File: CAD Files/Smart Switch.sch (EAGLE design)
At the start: 27 parts, among them IC1 78L05Z, X1 MKDSN1,5/3-5,08

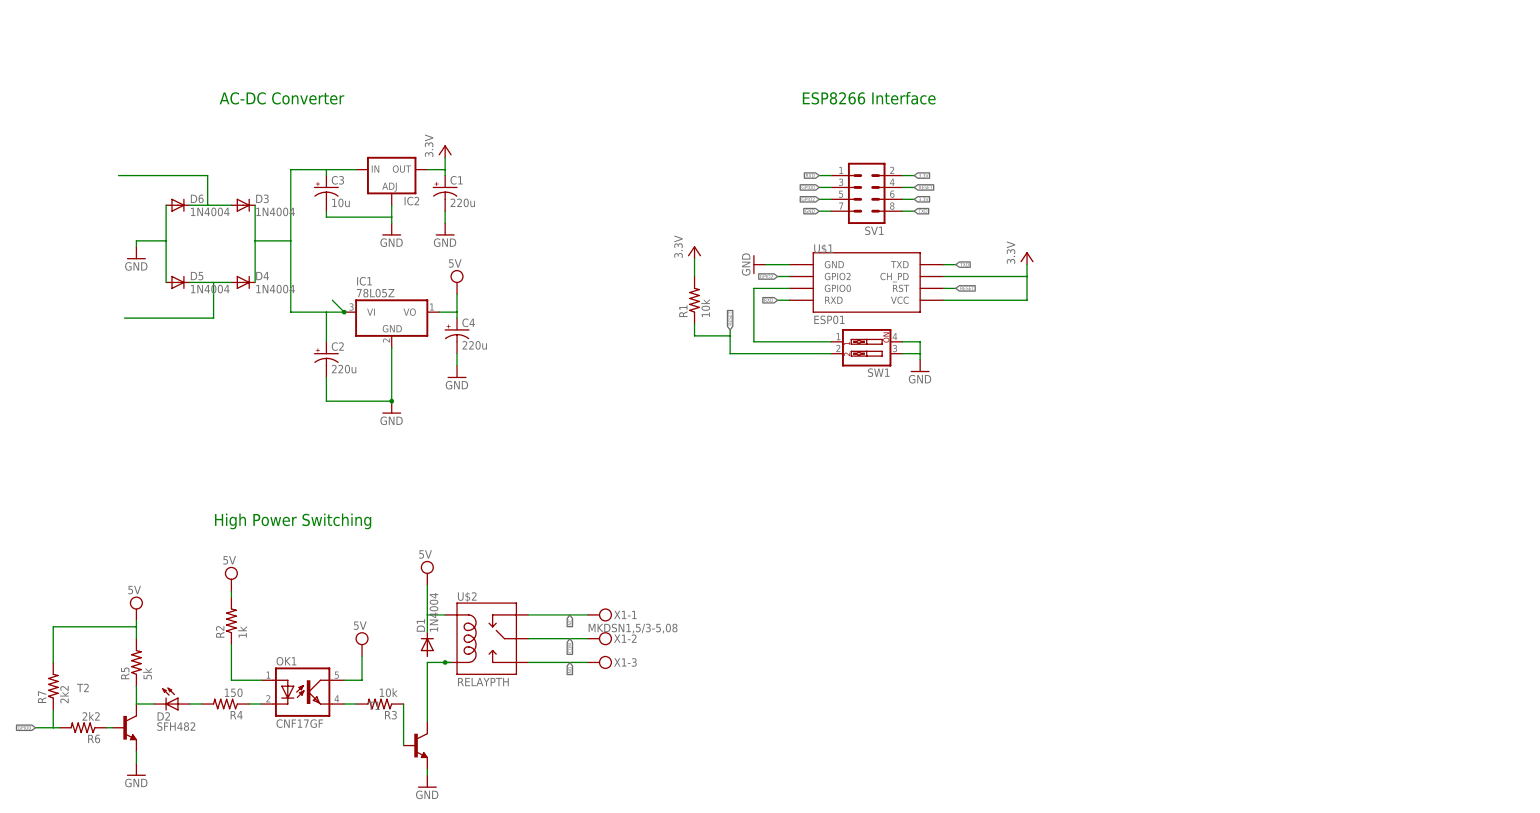
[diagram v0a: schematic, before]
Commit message: Added final schematic and board layout
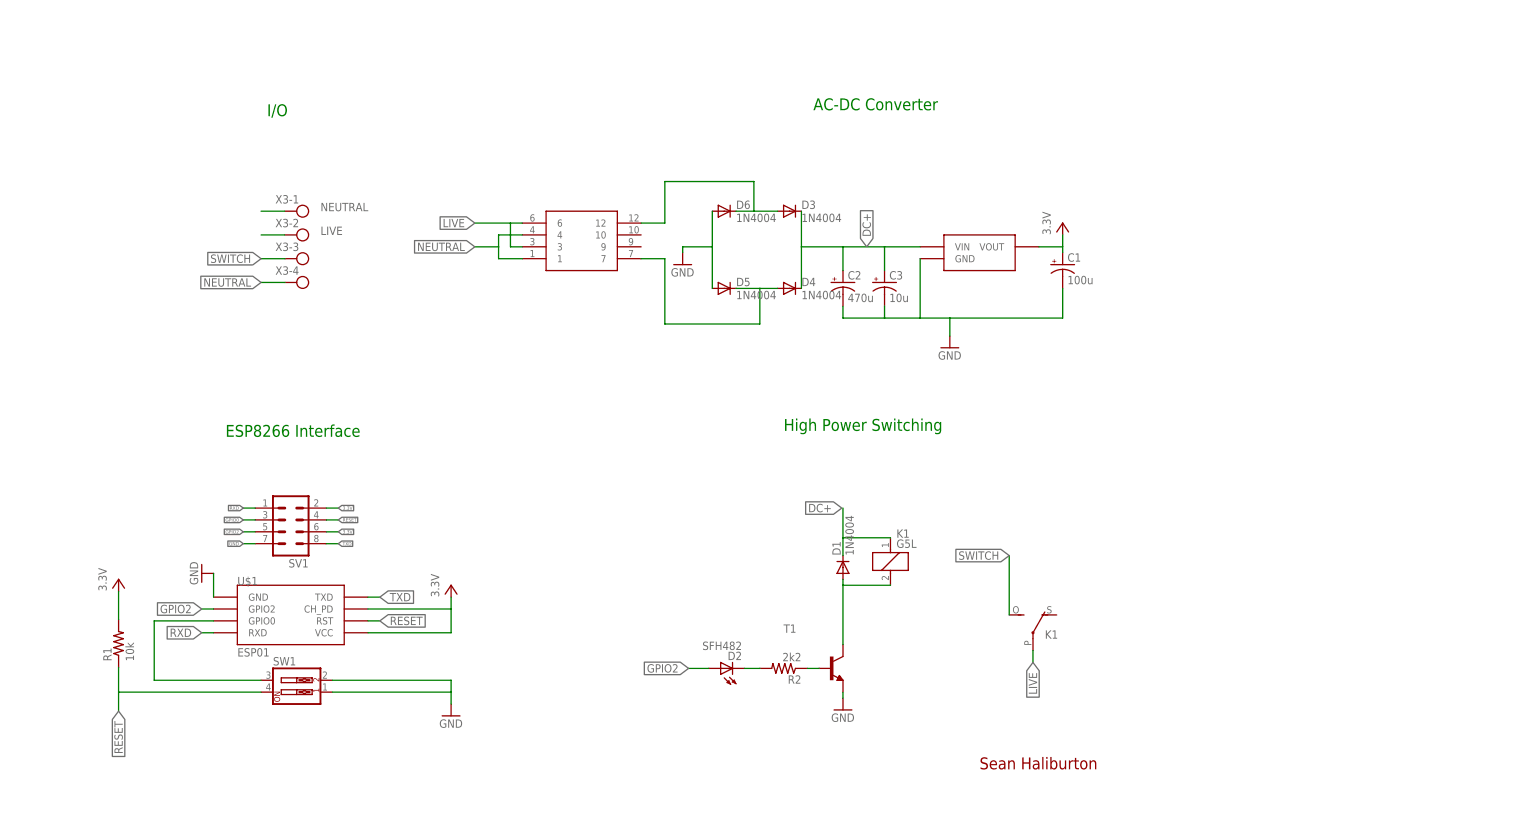
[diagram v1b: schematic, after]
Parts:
- removed C4: 220u, resistor:CPOL-USE2.5-6
- removed IC1: 78L05Z, linear:78L05Z
- removed IC2: (no value), v-reg:LM138-TL
- removed OK1: CNF17GF, optocoupler:CNF17GF
- removed R3: 10k, rcl:R-US_0411/15
- removed R4: 150, rcl:R-US_0411/15
- removed R5: 5k, rcl:R-US_0411/15
- removed R6, R7: 2k2, rcl:R-US_0411/15
- removed T2: (no value), transistor-neu-to92:2N2222-NPN-TO92-EBC
- removed X1: MKDSN1,5/3-5,08, con-phoenix-508:MKDSN1,5/3-5,08
- added K1: G5L, relay:G5L
- added U$3: CL2-10R-12, smart-switch:CL2-10R-12
- added X3: MKDSN1,5/4-5,08, con-phoenix-508:MKDSN1,5/4-5,08
- C1: value 220u -> 100u
- C2: value 220u -> 470u
- R1: device rcl:R-US_0411/15 -> rcl:R-US_0204/7
- R2: value 1k -> 2k2; device rcl:R-US_0411/15 -> rcl:R-US_0204/7
- U$2: value RELAYPTH -> ZLDO1117; device SRD-05VDC-SL-C:RELAYPTH -> smart-switch:ZLDO1117
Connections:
- removed net 3.3V1: C4.+
- removed net 5V: D1.C, IC1.VO, OK1.COL, R2.2, R5.2, R7.2, U$2.COIL1
- removed net COM: U$2.SWCOMMON, X1-2.KL
- removed net N$11: D3.A, D6.C
- removed net N$2: R3.1, T1.B
- removed net N$4: OK1.A, R2.1
- removed net N$6: OK1.C, R4.1
- removed net N$7: R6.1, T2.B
- removed net N$8: D4.A, D5.C
- removed net NC: U$2.SWCLOSE, X1-1.KL
- removed net NO: U$2.SWOPEN, X1-3.KL
- removed net X: D2.C, R5.1, T2.C
- new net LIVE: K12.P, U$3.3, U$3.6, X3-2.KL
- new net NEUTRAL: U$3.1, U$3.4, X3-1.KL, X3-4.KL
- new net SEC1: D3.A, D6.C, U$3.12
- new net SEC2: D4.A, D5.C, U$3.7
- new net SWITCH: K12.S, X3-3.KL
- net 3.3V: now also U$2.VOUT; no longer IC2.OUT
- net DC+: now also D1.C, K11.1, U$2.VIN; no longer IC1.VI, IC2.IN
- net GND: now also SW1.1, SW1.2, U$2.GND; no longer C4.-, IC1.GND, IC2.ADJ, SW1.3, SW1.4, T2.E
- net GPIO0: now also SW1.3; no longer R6.2, R7.1, SW1.1
- net GPIO2: now also D2.A
- net N$1: now also R2.1, T1.B; no longer OK1.EMIT, R3.2
- net N$3: now also D1.A, K11.2; no longer U$2.COIL0
- net N$5: now also D2.C, R2.2; no longer D2.A, R4.2
- net RESET: now also SW1.4; no longer SW1.2
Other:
- note added: "I/O"
- note added: "Sean Haliburton"
- moved on the sheet: C1, C2, C3, D1, D2, D3, D4, D5, D6, R1, R2, SV1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

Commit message: Changed most of the design
Replaced relay with triac and opto isolator
Replaced transformer with alternative AC-DC converter
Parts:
- removed D1, D3, D4, D5, D6: 1N4004, diode:1N4004
- removed K1: G5L, relay:G5L
- removed T1: (no value), transistor-neu-to92:2N2222-NPN-TO92-EBC
- removed U$3: CL2-10R-12, smart-switch:CL2-10R-12
- added B1: (no value), rectifier:B-DIL
- added CX1: 0.6u, rcl:CXXC10B6
- added OK1: MOC3020M, optocoupler:MOC3020M
- added R3: 1M, rcl:R-US_0204/7
- added R4, R5: 100, rcl:R-US_0204/7
- added R6: (no value), rcl:R-US_0204/7
- added R7: 200, rcl:R-US_0204/7
- added T2: BTA26-H, triac:BTA26-H
- C2: value 470u -> 1000u
- D2: value SFH482 -> (none); device led:SFH482 -> diode:ZENER-DIODEP1-12
- R2: value 2k2 -> 100
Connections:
- removed net N$3: D1.A, K11.2, T1.C
- removed net SEC2: D4.A, D5.C, U$3.7
- new net N$2: CX1.1, R3.2, R4.1
- new net N$4: C3.+, D2.C, R5.1, U$2.VIN
- new net N$6: R7.2, T2.G
- net DC+: now also B1.+, R5.2; no longer C3.+, D1.C, D3.C, D4.C, K11.1, U$2.VIN
- net GND: now also B1.-, D2.A, R2.2; no longer D5.A, D6.A, T1.E
- net GPIO0: now also OK1.A
- net GPIO2: no longer D2.A
- net LIVE: now also OK1.A2, R4.2, T2.A2; no longer K12.P, U$3.3, U$3.6
- net N$1: now also OK1.C; no longer T1.B
- net N$5: now also OK1.A1, R7.1; no longer D2.C, R2.2
- net NEUTRAL: now also B1.AC2; no longer U$3.1, U$3.4
- net SEC1: now also B1.AC1, CX1.2, R3.1; no longer D3.A, D6.C, U$3.12
- net SWITCH: now also T2.A1; no longer K12.S
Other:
- moved on the sheet: C1, C2, C3, R1, R2

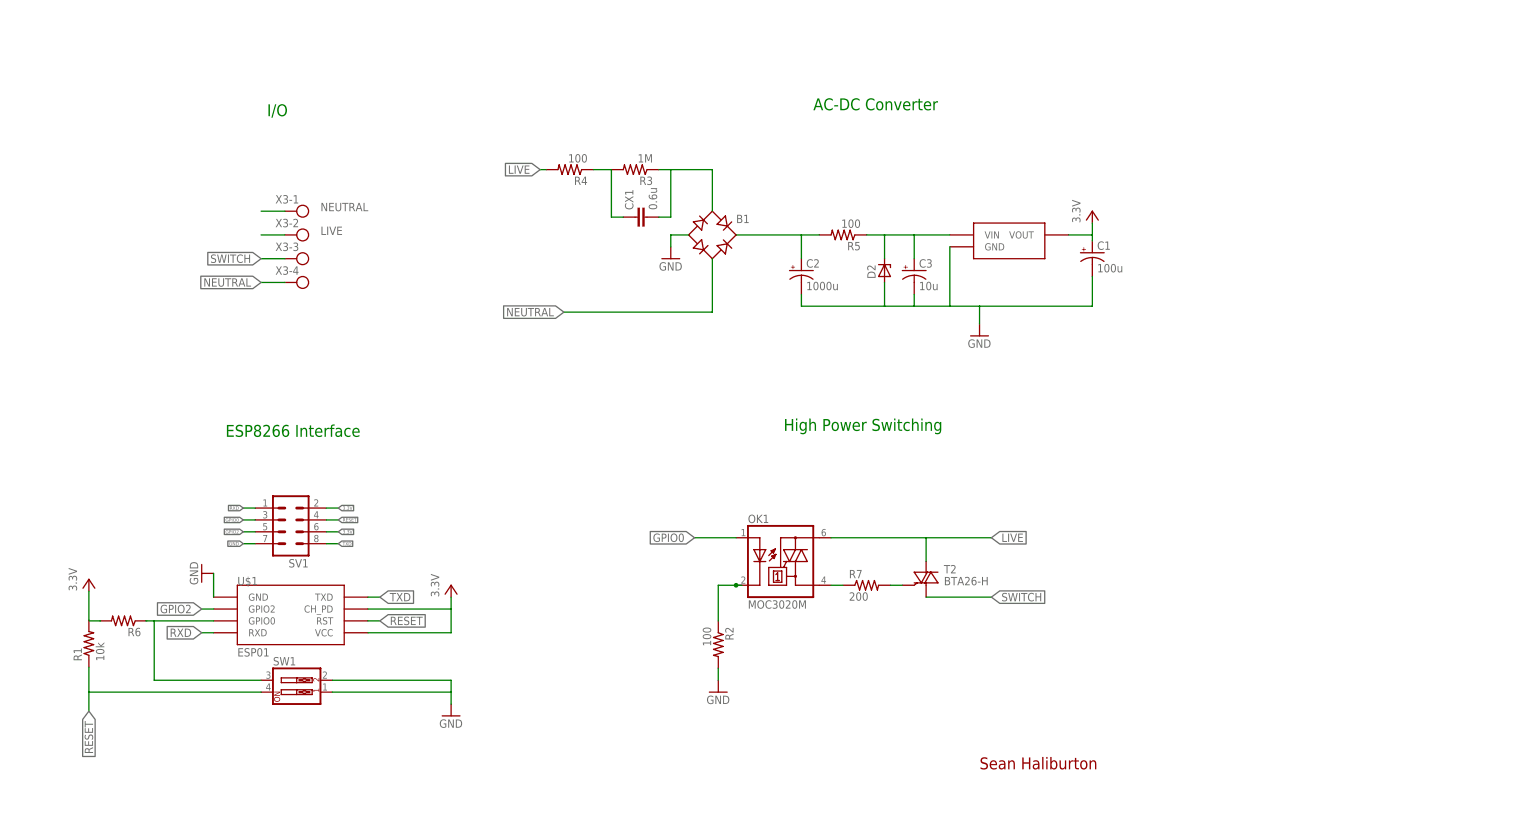
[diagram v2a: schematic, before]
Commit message: Revision was sent for manufacturing
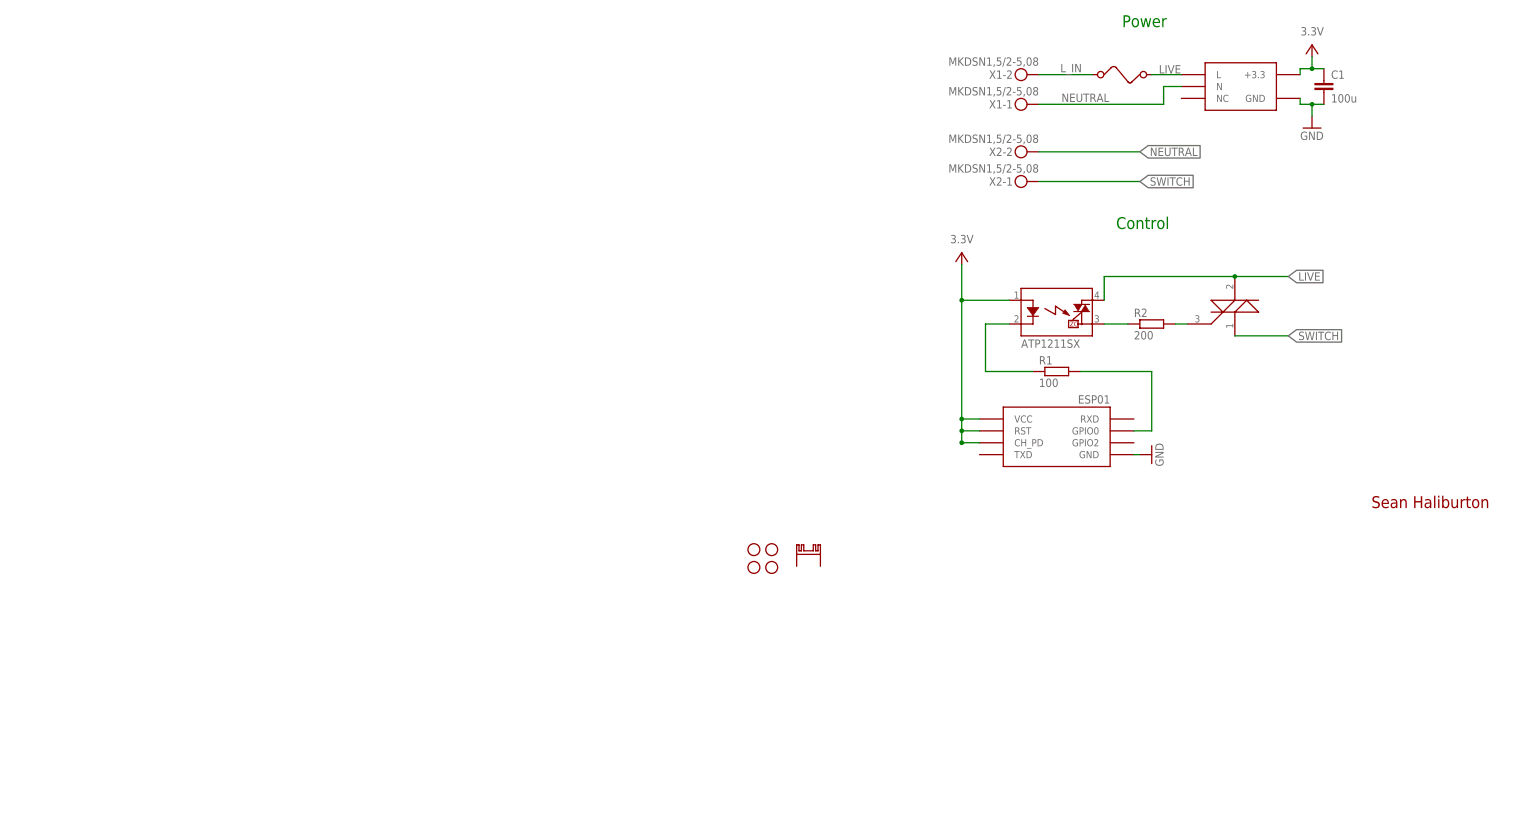
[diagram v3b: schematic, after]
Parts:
- removed B1: (no value), rectifier:B-DIL
- removed C2: 1000u, resistor:CPOL-USE2.5-6
- removed C3: 10u, resistor:CPOL-USE2.5-6
- removed CX1: 0.6u, rcl:CXXC10B6
- removed D2: (no value), diode:ZENER-DIODEP1-12
- removed OK1: MOC3020M, optocoupler:MOC3020M
- removed R3: 1M, rcl:R-US_0204/7
- removed R4, R5: 100, rcl:R-US_0204/7
- removed R6: (no value), rcl:R-US_0204/7
- removed R7: 200, rcl:R-US_0204/7
- removed SV1: (no value), con-lstb:MA04-2
- removed SW1: (no value), special:SW_DIP-2
- removed T2: BTA26-H, triac:BTA26-H
- removed X3: MKDSN1,5/4-5,08, con-phoenix-508:MKDSN1,5/4-5,08
- added H1, H2, H3, H4: STAND-OFF, SparkFun-Hardware:STAND-OFF
- added K1: ATP1211SX, relay:ATP1211SX
- added U$3: BTA16, smart-switch:BTA16
- added U$4: FUSE, smart-switch:FUSE
- added U$5: RA-T2X-38E, smart-switch:RA-T2X-38E
- added X1, X2: MKDSN1,5/2-5,08, con-phoenix-508:MKDSN1,5/2-5,08
- C1: device resistor:CPOL-USE2.5-6 -> resistor:C-EUC0805
- R1: value 10k -> 100; device rcl:R-US_0204/7 -> resistor:R-EU_R0805
- R2: value 100 -> 200; device rcl:R-US_0204/7 -> resistor:R-EU_R0805
- U$2: value ZLDO1117 -> RAC04-GB; device smart-switch:ZLDO1117 -> smart-switch:RAC04-GB
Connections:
- removed net 3.3V: C1.+, R1.2, SV1.2, SV1.6, U$1.CH_PD, U$1.VCC, U$2.VOUT
- removed net DC+: B1.+, C2.+, R5.2
- removed net GPIO2: SV1.5, U$1.GPIO2
- removed net N$2: CX1.1, R3.2, R4.1
- removed net N$4: C3.+, D2.C, R5.1, U$2.VIN
- removed net RESET: R1.1, SV1.4, SW1.4, U$1.RST
- removed net RXD: SV1.1, U$1.RXD
- removed net SEC1: B1.AC1, CX1.2, R3.1
- removed net TXD: SV1.8, U$1.TXD
- new net L_IN: U$4.1, X1-2.KL
- new net VCC: C1.1, K1.A, U$1.CH_PD, U$1.RST, U$1.VCC, U$2.+3.3
- net GND: now also C1.2; no longer B1.-, C1.-, C2.-, C3.-, D2.A, R2.2, SV1.7, SW1.1, SW1.2
- net GPIO0: now also R1.2; no longer OK1.A, SV1.3, SW1.3
- net LIVE: now also K1.DS1, U$2.L, U$3.A2, U$4.2; no longer OK1.A2, R4.2, T2.A2, X3-2.KL
- net N$1: now also K1.K, R1.1; no longer OK1.C, R2.1
- net N$5: now also K1.DS2, R2.1; no longer OK1.A1, R7.1
- net N$6: now also R2.2, U$3.G; no longer R7.2, T2.G
- net NEUTRAL: now also U$2.N, X1-1.KL, X2-2.KL; no longer B1.AC2, X3-1.KL, X3-4.KL
- net SWITCH: now also U$3.A1, X2-1.KL; no longer T2.A1, X3-3.KL
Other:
- note added: "Control"
- note added: "Power"
- note removed: "AC-DC Converter"
- note removed: "ESP8266 Interface"
- note removed: "High Power Switching"
- note removed: "I/O"
